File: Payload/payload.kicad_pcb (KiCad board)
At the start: 4 copper layers, 75 x 40 mm, 48 parts, among them J1 Conn_ARM_JTAG_SWD_10, J2 Conn_01x02, J3 Conn_01x02, J4 Conn_01x08, J5 Conn_02x13_Counter_Clockwise, Q1 Q_PMOS_GSD, SW1 SW_SPST, U1 STM32L471RGTx, U2 ISO1541, U3 MAX6371, U4 CY62167EV30LL, U5 CY62167EV30LL, U6 CY62167EV30LL

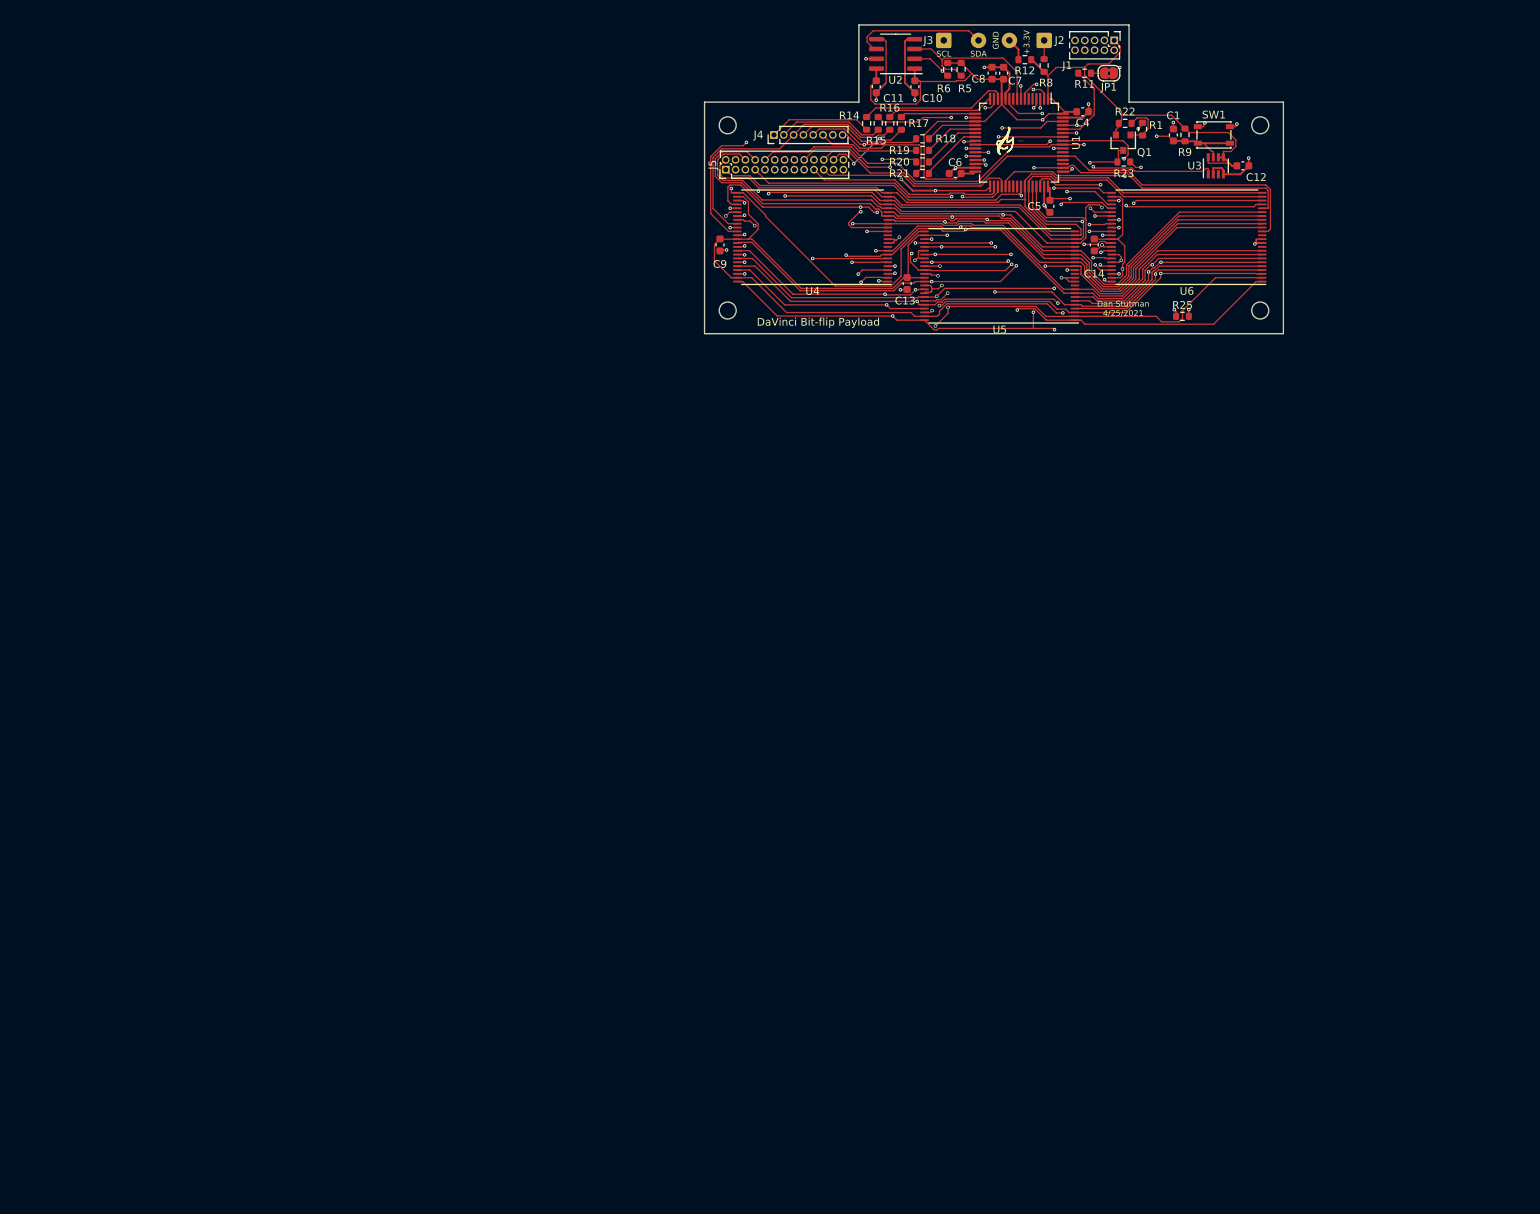
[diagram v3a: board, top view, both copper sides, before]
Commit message: Correct silk violations
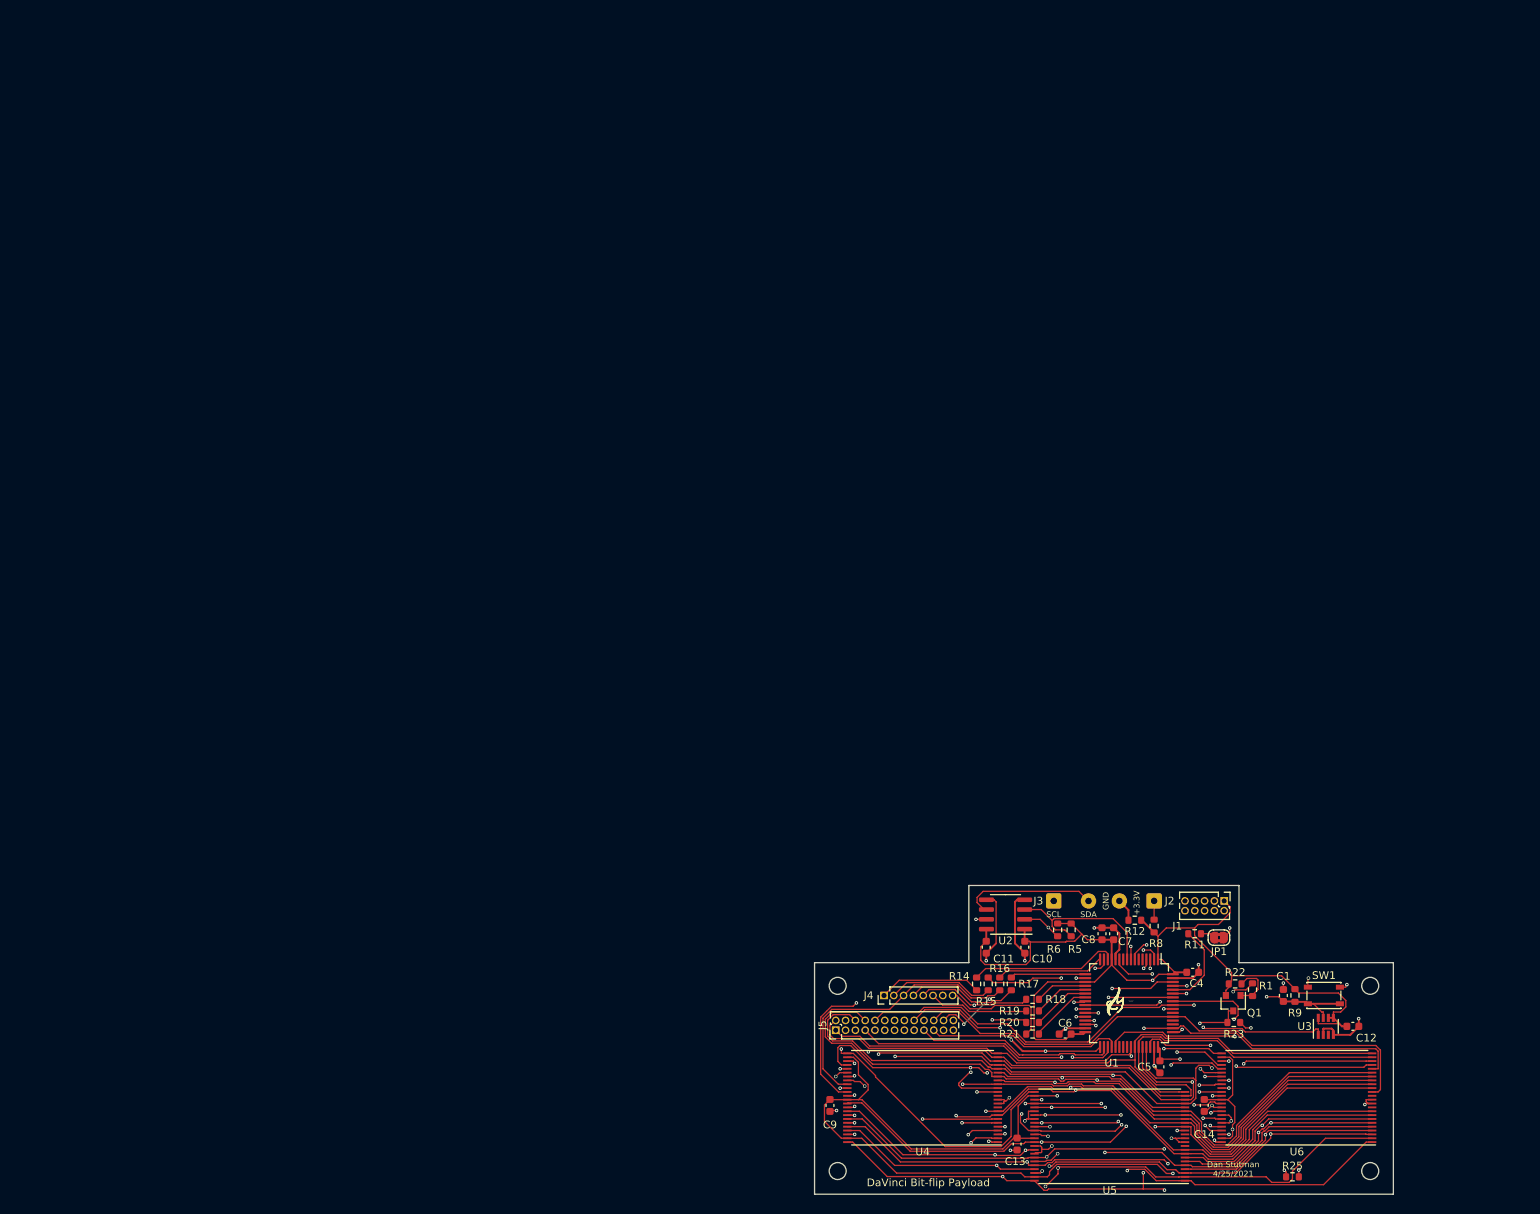
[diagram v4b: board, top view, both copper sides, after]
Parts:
- removed the REF** at (172.0, -22.0)
- removed the REF** at (172.0, 2.00)
- removed the REF** at (103.0, 2.00)
- added REF**: MountingHole_2.2mm_M2, MountingHole:MountingHole_2.2mm_M2, F.Cu at (186.2, 89.5)
- added REF**: MountingHole_2.2mm_M2, MountingHole:MountingHole_2.2mm_M2, F.Cu at (186.2, 113.5)
- added REF**: MountingHole_2.2mm_M2, MountingHole:MountingHole_2.2mm_M2, F.Cu at (117.2, 113.5)
- moved JP1 112.9 mm to (166.7, 83.2)
- moved C1 112.4 mm to (175.0, 90.8)
- moved C10 112.4 mm to (141.5, 84.5)
- moved C11 112.4 mm to (136.5, 84.5)
- moved C12 112.4 mm to (184.0, 94.8)
- moved C13 112.4 mm to (140.5, 110.0)
- moved C14 112.4 mm to (164.8, 105.0)
- moved C4 112.4 mm to (163.2, 87.8)
- moved C5 112.4 mm to (159.0, 100.0)
- moved C6 112.4 mm to (146.7, 95.8)
- moved C7 112.4 mm to (153.0, 82.8)
- moved C8 112.4 mm to (151.5, 82.8)
- moved C9 112.4 mm to (116.2, 105.0)
- moved J1 112.4 mm to (167.3, 78.5)
- moved J2 112.4 mm to (158.2, 78.5)
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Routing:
- net Net-(R1-Pad1): track 25.3 -> 26.4 mm
- net Net-(R6-Pad2): track 17.8 -> 18.6 mm

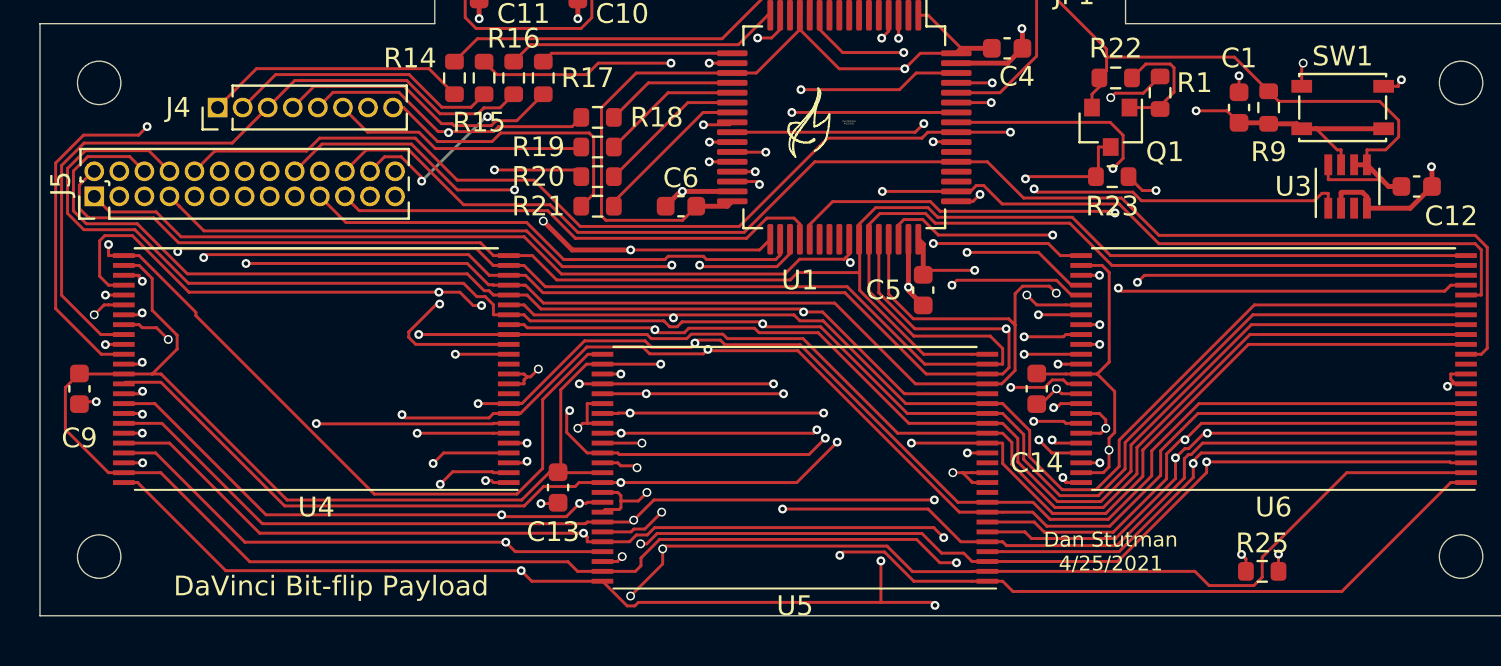
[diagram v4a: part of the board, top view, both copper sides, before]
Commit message: Modify silk
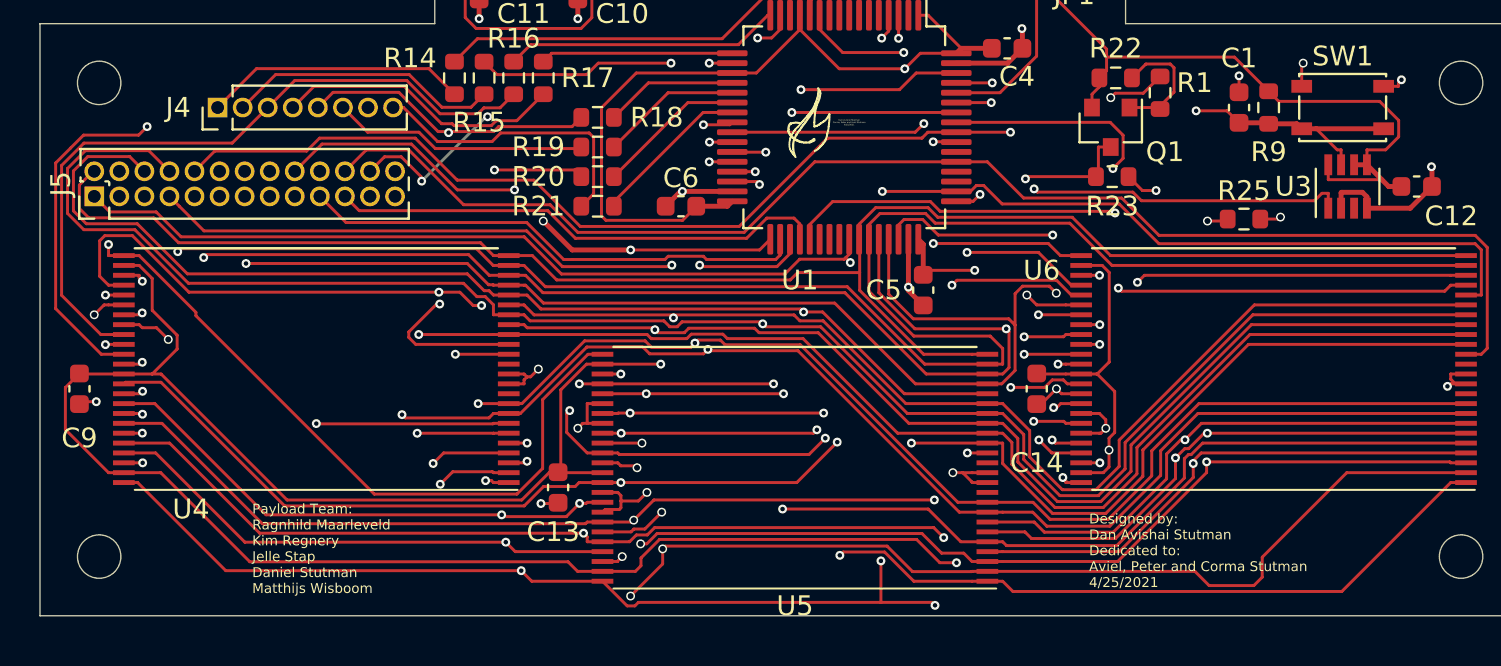
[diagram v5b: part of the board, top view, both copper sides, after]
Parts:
- moved R25 17.9 mm to (175.2, 96.4)
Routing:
- net Net-(C13-Pad2): track 170.0 -> 166.1 mm
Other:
- board text added: "Dan Avishai Stutman Corma, Peter and Aviel Stutman 4/25/2021"
- board text added: "Designed by: Dan Avishai Stutman Dedicated to: Aviel, Peter and Corma Stutman 4/25/2021"
- board text added: "Payload Team: Ragnhild Maarleveld Kim Regnery Jelle Stap Daniel Stutman Matthijs Wisboom"
- board text removed: "Dan Stutman 4/25/2021"

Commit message: Update component values and isolator
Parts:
- R1: value R_Small_US -> 200 R
- R23: value R_Small_US -> 100
- R8: value 55 R -> 43 R
- U2: value ISO1541 -> ISO1540

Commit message: Tweak
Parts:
- R12: value 100 K -> 100 kR
- R23: value 100 -> 100 R
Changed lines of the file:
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@@
       (effects (font (size 1 1) (thickness 0.15)))
     )
-    (fp_text value 100 (at 0 1.43) (layer F.Fab)
+    (fp_text value "100 R" (at 0 1.43) (layer F.Fab)
       (effects (font (size 1 1) (thickness 0.15)))
     )
@@
       (effects (font (size 1 1) (thickness 0.15)))
     )
-    (fp_text value "100 K" (at 0 1.43) (layer F.Fab)
+    (fp_text value "100 kR" (at 0 1.43) (layer F.Fab)
       (effects (font (size 1 1) (thickness 0.15)))
     )
@@
     )
   )
-  (gr_text "Designed by:\nDan Avishai Stutman\nDedicated to:\nAviel, Peter and Corma Stutman\n4/25/2021" (at 167.4 113.2) (layer F.SilkS)
+  (gr_text "Payload Team:\nRagnhild Maarleveld\nKim Regnery\nJelle Stap\nDaniel Stutman\nMatthijs Wisboom" (at 124.1 113.3) (layer F.SilkS)
     (effects (font (size 0.5 0.5) (thickness 0.1)) (justify left))
+  )
+  (gr_text "Designed by:\nDan Avishai Stutman\nDedicated to:\nAviel, Peter and Corma Stutman\n4/25/2021" (at 167.4 112.9) (layer F.SilkS)
+    (effects (font (size 0.5 0.5) (thickness 0.1)) (justify left))
+  )
+  (gr_text "Dan Avishai Stutman\nCorma, Peter and Aviel Stutman\n4/25/2021" (at 155.25 91.5) (layer F.SilkS)
+    (effects (font (size 0.075 0.075) (thickness 0.01875)))
   )
   (gr_curve (pts (xy 154.231 91.16) (xy 154.24 91.16) (xy 154.224 91.497) (xy 154.213 91.547)) (layer F.SilkS) (width 0.02))
@@
     (effects (font (size 1 1) (thickness 0.15)) (justify mirror))
   )
-  (gr_text "Payload Team:\nRagnhild Maarleveld\nKim Regnery\nJelle Stap\nDaniel Stutman\nMatthijs Wisboom" (at 125 113.1) (layer F.SilkS)
-    (effects (font (size 0.5 0.5) (thickness 0.1)) (justify left))
-  )
-  (gr_text "Dan Avishai Stutman\nCorma, Peter and Aviel Stutman\n4/25/2021" (at 155.25 91.5) (layer F.SilkS)
-    (effects (font (size 0.075 0.075) (thickness 0.01875)))
-  )
   (gr_line (start 114.25 86.5) (end 114.25 116.5) (layer Edge.Cuts) (width 0.05))
